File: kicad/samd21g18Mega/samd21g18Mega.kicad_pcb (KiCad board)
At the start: 2 copper layers, 101.6 x 53.3 mm, 12 parts, among them P1 Digital, P10 CONN_01X01, P11 CONN_01X01, P13 CONN_01X01, P2 Power, P3 Analog, P4 Analog, P5 PWM, P6 PWM, P7 Communication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

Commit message: samd21 mega and whole deck cut grx
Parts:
- added U2: L7805, Package_TO_SOT_THT:TO-220-3_Horizontal_TabDown, F.Cu at (107.3, 76.8)
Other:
- board text added: "Tab is down on AZ2940 (here shown as a 7805)"
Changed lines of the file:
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@@
   (general
     (thickness 1.6)
-    (drawings 10)
+    (drawings 11)
     (tracks 0)
     (zones 0)
-    (modules 12)
-    (nets 133)
+    (modules 13)
+    (nets 136)
   )
   (page A4)
@@
   (net 131 "Net-(U1-Pad25)")
   (net 132 "Net-(U1-Pad1)")
+  (net 133 "Net-(U2-Pad3)")
+  (net 134 "Net-(U2-Pad2)")
+  (net 135 "Net-(U2-Pad1)")
   (net_class Default "This is the default net class."
     (clearance 0.2)
@@
     (add_net "Net-(U1-Pad8)")
     (add_net "Net-(U1-Pad9)")
+    (add_net "Net-(U2-Pad1)")
+    (add_net "Net-(U2-Pad2)")
+    (add_net "Net-(U2-Pad3)")
+  )
+  (module Package_TO_SOT_THT:TO-220-3_Horizontal_TabDown (layer F.Cu)
+    (at 107.315 76.835 270)
+    (descr "TO-220-3, Horizontal, RM 2.54mm, see https://www.vishay.com/docs/66542/to-220-1.pdf")
+    (tags "TO-220-3 Horizontal RM 2.54mm")
+    (fp_text reference U2 (at 2.54 20.58 90) (layer F.SilkS)
+      (effects (font (size 1 1) (thickness 0.15)))
+    )
+    (fp_text value L7805 (at 2.54 -2 90) (layer F.Fab)
+      (effects (font (size 1 1) (thickness 0.15)))
+    )
+    (fp_text user %R (at 2.54 20.58 90) (layer F.Fab)
+      (effects (font (size 1 1) (thickness 0.15)))
+    )
+    (fp_line (start 7.79 -19.71) (end -2.71 -19.71) (layer F.CrtYd) (width 0.05))
+    (fp_line (start 7.79 1.25) (end 7.79 -19.71) (layer F.CrtYd) (width 0.05))
+    (fp_line (start -2.71 1.25) (end 7.79 1.25) (layer F.CrtYd) (width 0.05))
+    (fp_line (start -2.71 -19.71) (end -2.71 1.25) (layer F.CrtYd) (width 0.05))
+    (fp_line (start 5.08 -3.69) (end 5.08 -1.15) (layer F.SilkS) (width 0.12))
+    (fp_line (start 2.54 -3.69) (end 2.54 -1.15) (layer F.SilkS) (width 0.12))
+    (fp_line (start 0 -3.69) (end 0 -1.15) (layer F.SilkS) (width 0.12))
+    (fp_line (start 7.66 -19.58) (end 7.66 -3.69) (layer F.SilkS) (width 0.12))
+    (fp_line (start -2.58 -19.58) (end -2.58 -3.69) (layer F.SilkS) (width 0.12))
+    (fp_line (start -2.58 -19.58) (end 7.66 -19.58) (layer F.SilkS) (width 0.12))
+    (fp_line (start -2.58 -3.69) (end 7.66 -3.69) (layer F.SilkS) (width 0.12))
+    (fp_line (start 5.08 -3.81) (end 5.08 0) (layer F.Fab) (width 0.1))
+    (fp_line (start 2.54 -3.81) (end 2.54 0) (layer F.Fab) (width 0.1))
+    (fp_line (start 0 -3.81) (end 0 0) (layer F.Fab) (width 0.1))
+    (fp_line (start 7.54 -3.81) (end -2.46 -3.81) (layer F.Fab) (width 0.1))
+    (fp_line (start 7.54 -13.06) (end 7.54 -3.81) (layer F.Fab) (width 0.1))
+    (fp_line (start -2.46 -13.06) (end 7.54 -13.06) (layer F.Fab) (width 0.1))
+    (fp_line (start -2.46 -3.81) (end -2.46 -13.06) (layer F.Fab) (width 0.1))
+    (fp_line (start 7.54 -13.06) (end -2.46 -13.06) (layer F.Fab) (width 0.1))
+    (fp_line (start 7.54 -19.46) (end 7.54 -13.06) (layer F.Fab) (width 0.1))
+    (fp_line (start -2.46 -19.46) (end 7.54 -19.46) (layer F.Fab) (width 0.1))
+    (fp_line (start -2.46 -13.06) (end -2.46 -19.46) (layer F.Fab) (width 0.1))
+    (fp_circle (center 2.54 -16.66) (end 4.39 -16.66) (layer F.Fab) (width 0.1))
+    (pad 3 thru_hole oval (at 5.08 0 270) (size 1.905 2) (drill 1.1) (layers *.Cu *.Mask)
+      (net 133 "Net-(U2-Pad3)"))
+    (pad 2 thru_hole oval (at 2.54 0 270) (size 1.905 2) (drill 1.1) (layers *.Cu *.Mask)
+      (net 134 "Net-(U2-Pad2)"))
+    (pad 1 thru_hole rect (at 0 0 270) (size 1.905 2) (drill 1.1) (layers *.Cu *.Mask)
+      (net 135 "Net-(U2-Pad1)"))
+    (pad "" np_thru_hole oval (at 2.54 -16.66 270) (size 3.5 3.5) (drill 3.5) (layers *.Cu *.Mask))
+    (model ${KISYS3DMOD}/Package_TO_SOT_THT.3dshapes/TO-220-3_Horizontal_TabDown.wrl
+      (at (xyz 0 0 0))
+      (scale (xyz 1 1 1))
+      (rotate (xyz 0 0 0))
+    )
   )
   (module Package_DIP:DIP-48_W15.24mm (layer F.Cu)
@@
       (net 74 "Net-(P13-Pad1)"))
   )
+  (gr_text "Tab is down on AZ2940 (here shown as a 7805)" (at 146.685 79.375) (layer Dwgs.User)
+    (effects (font (size 1 1) (thickness 0.15)))
+  )
   (gr_text 1 (at 131.318 116.586 90) (layer F.SilkS)

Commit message: cut for deal partly done
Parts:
- added P12: CONN_01X01, Socket_Arduino_Mega:Arduino_1pin, F.Cu at (94.0, 97.2)
- added P9: CONN_01X01, Socket_Arduino_Mega:Arduino_1pin, F.Cu at (88.3, 97.2)
- U2: footprint Package_TO_SOT_THT:TO-220-3_Horizontal_TabDown -> Package_TO_SOT_THT:TO-220-3_Horizontal_TabUp
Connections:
- U1 pad 10: Net-(U1-Pad10) -> /A4
- U1 pad 11: Net-(U1-Pad11) -> /8(**)
- U1 pad 12: Net-(U1-Pad12) -> /9(**)
- U1 pad 13: Net-(U1-Pad13) -> /4(**)
- U1 pad 14: Net-(U1-Pad14) -> /3(**)
- U1 pad 15: Net-(U1-Pad15) -> /1(Tx0)
- U1 pad 16: Net-(U1-Pad16) -> /0(Rx0)
- U1 pad 23: Net-(U1-Pad23) -> /2(**)
- U1 pad 24: Net-(U1-Pad24) -> /5(**)
- U1 pad 25: Net-(U1-Pad25) -> /11(**)
- U1 pad 26: Net-(U1-Pad26) -> /13(**)
- U1 pad 27: Net-(U1-Pad27) -> /10(**)
- U1 pad 28: Net-(U1-Pad28) -> /12(**)
- U1 pad 29: Net-(U1-Pad29) -> /6(**)
- U1 pad 3: Net-(U1-Pad3) -> /A0
- U1 pad 30: Net-(U1-Pad30) -> /7(**)
- U1 pad 47: Net-(U1-Pad47) -> /A5
- U1 pad 7: Net-(U1-Pad7) -> /A1
- U1 pad 8: Net-(U1-Pad8) -> /A2
- U1 pad 9: Net-(U1-Pad9) -> /A3

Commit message: sd21g18mega soldering guide, dealmode rough
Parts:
- moved U2 36.7 mm to (118.7, 111.8), turned to 90 degrees
- moved U1 5.43 mm to (118.7, 100.3)
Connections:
- U1 pad 17: Net-(U1-Pad17) -> +3V3
- U1 pad 18: Net-(U1-Pad18) -> GND
- U1 pad 35: Net-(U1-Pad35) -> GND
- U1 pad 36: Net-(U1-Pad36) -> +3V3
- U1 pad 42: Net-(U1-Pad42) -> GND
- U1 pad 44: Net-(U1-Pad44) -> +3V3
- U1 pad 5: Net-(U1-Pad5) -> GND
- U1 pad 6: Net-(U1-Pad6) -> +3V3
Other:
- board text added: "+5V"
- board text added: "3V3"
- board text added: "A0"
- board text added: "A1"
- board text added: "A2"
- board text added: "A3"
- board text added: "A4"
- board text added: "A5"
- board text added: "AREF"
- board text added: "D+"
- board text added: "D-"
- board text added: "D0"
- board text added: "D1"
- board text added: "D10"
- board text added: "D11"
- board text added: "D12"
- board text added: "D13"
- board text added: "D2"
- board text added: "D3"
- board text added: "D4"
- board text added: "D5"
- board text added: "D6"
- board text added: "D7"
- board text added: "D8"
- board text added: "D9"
- board text added: "FlshCS"
- board text added: "FlshMISO"
- board text added: "FlshMOSI"
- board text added: "FlshSCK"
- board text added: "GND"
- board text added: "IOREF"
- board text added: "MISO"
- board text added: "MOSI"
- board text added: "PixClk"
- board text added: "PixData"
- board text added: "RESET"
- board text added: "SCK"
- board text added: "SCL"
- board text added: "SDA"
- board text added: "SWCLK"
- board text added: "SWDIO"
- board text added: "VIN"
- board text added: "~RESET"

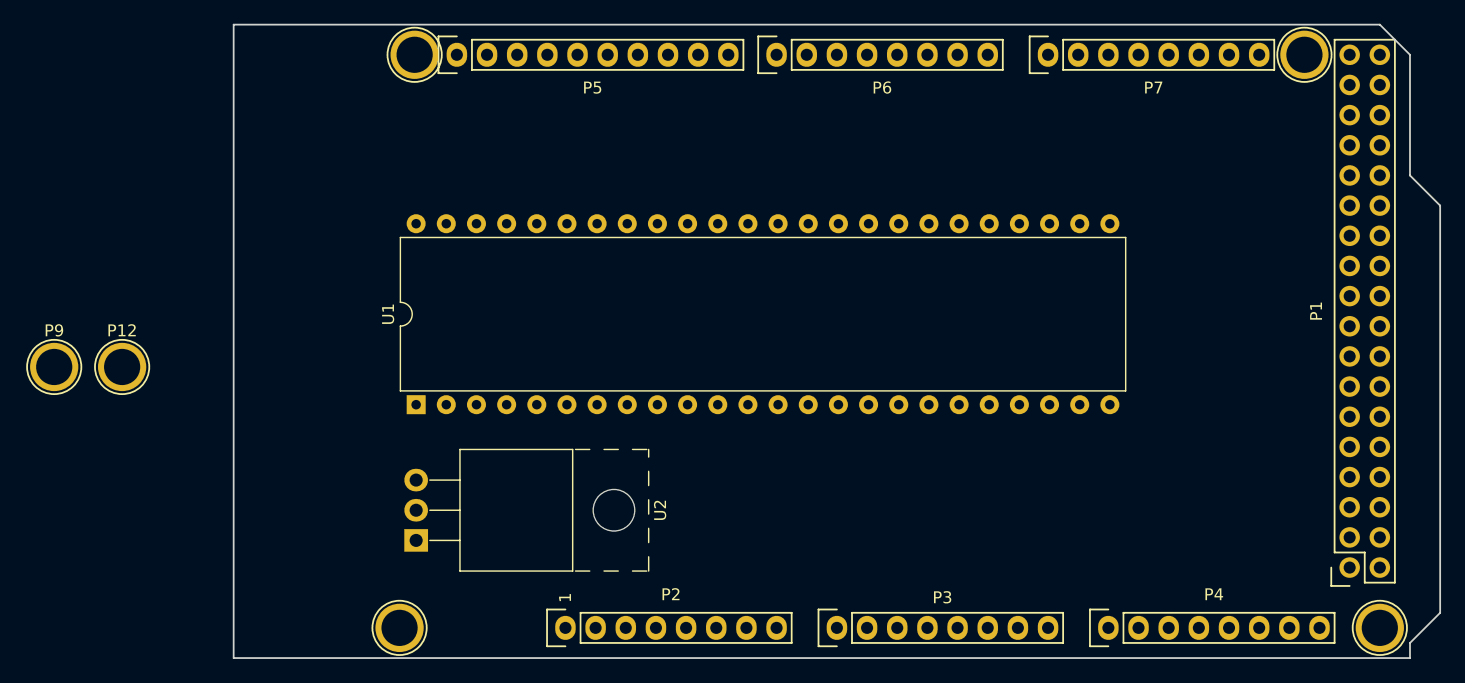
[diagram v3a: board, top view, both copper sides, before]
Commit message: rewrote pybbage shuffle
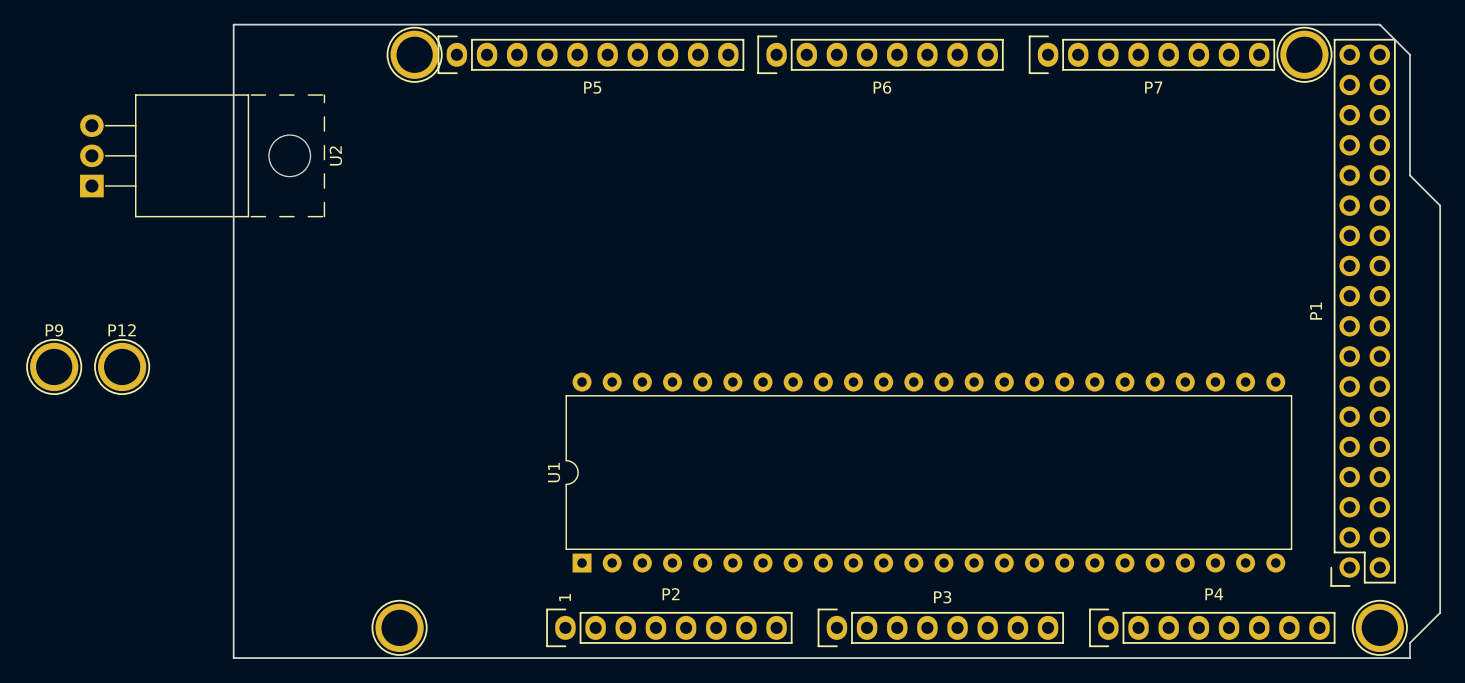
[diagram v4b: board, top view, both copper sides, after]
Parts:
- moved U2 40.5 mm to (91.4, 81.9)
- moved U1 19.3 mm to (132.7, 113.7)
